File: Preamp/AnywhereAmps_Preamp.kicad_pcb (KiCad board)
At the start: 2 copper layers, 69.1 x 45.2 mm, 59 parts, among them J1 +9V, J2 Battery, J3 VCC, J4 Switch, J5 Pwr LED, J6 POTI, J7 Audio_In, J8 Audio_Out, U1 PTPSM5601R5H, U2 MAX17562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

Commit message: add OSHW logo
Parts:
- added REF**: OSHW-Logo2_9.8x8mm_SilkScreen, Symbol:OSHW-Logo2_9.8x8mm_SilkScreen, F.Cu at (106.9, 141.2)

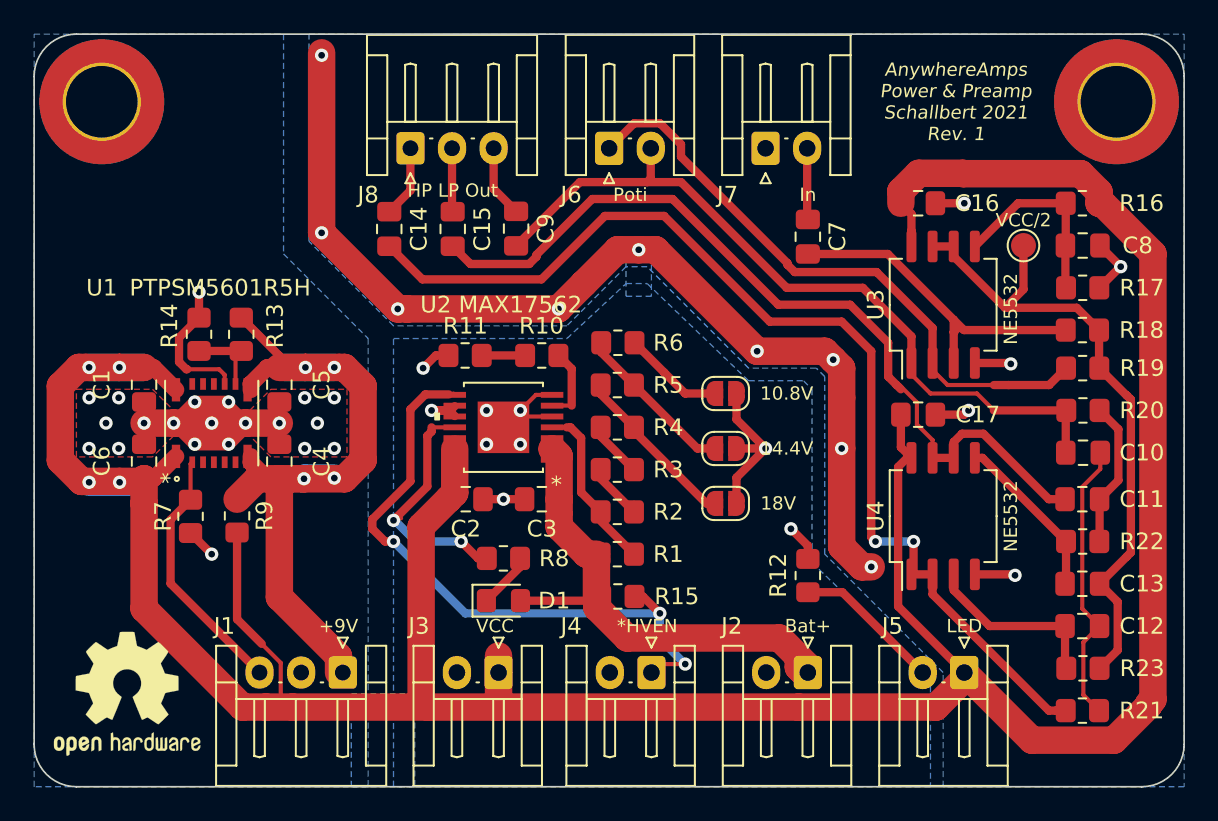
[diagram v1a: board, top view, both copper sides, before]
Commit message: - increate power track size to 2mm - reduce amount of right angles in track design
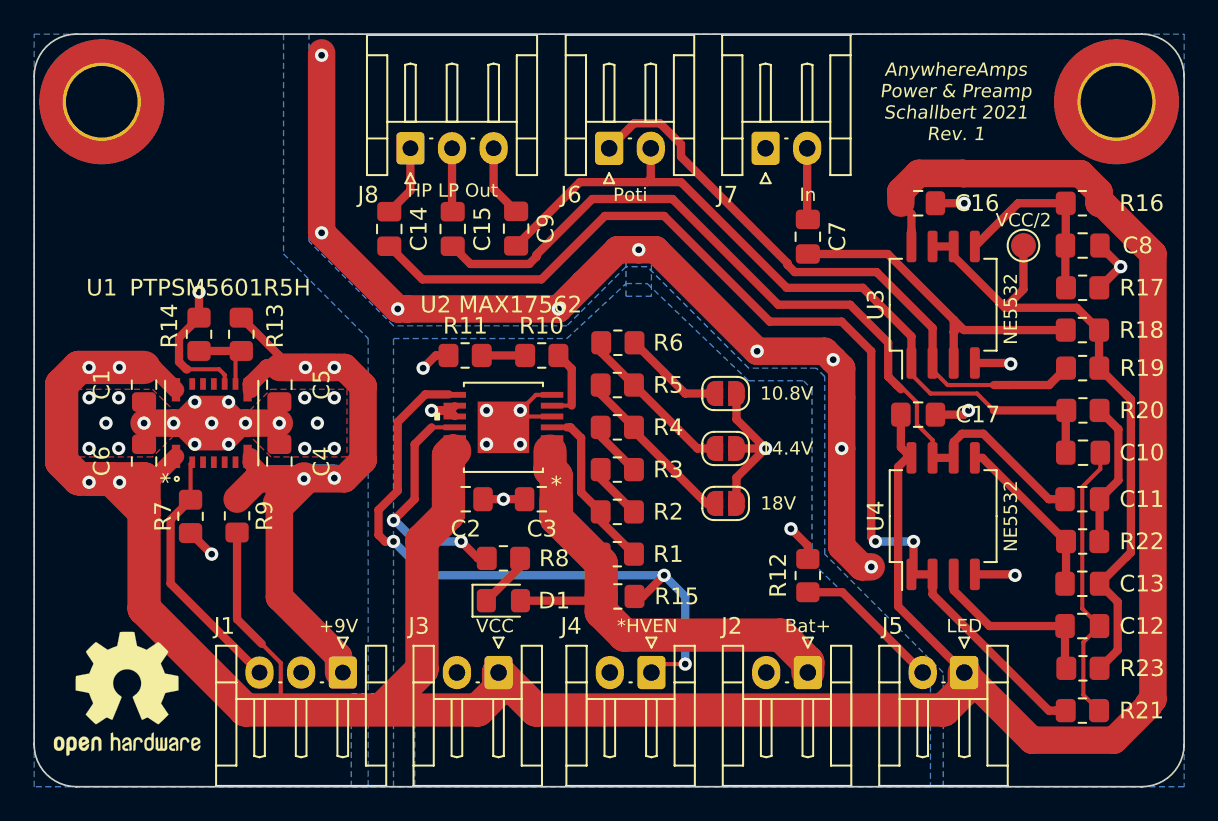
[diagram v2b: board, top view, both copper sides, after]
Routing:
- net VCC: track 202.8 -> 207.2 mm
- net +9V: track 46.8 -> 48.9 mm
- net +BATT: track 33.0 -> 31.1 mm
- net *HVEN: track 38.4 -> 39.8 mm

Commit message: - more 45° edging - update silk screen
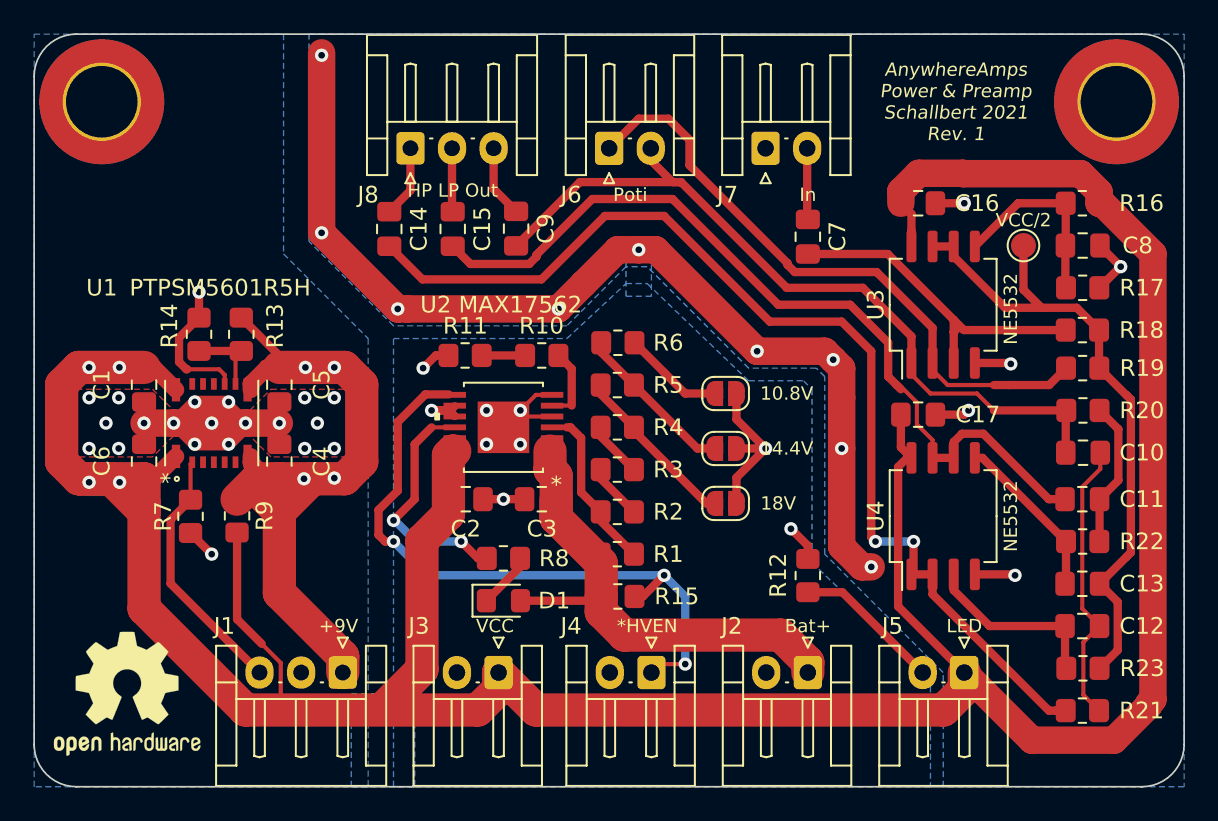
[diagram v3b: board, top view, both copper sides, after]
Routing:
- net +9V: track 48.9 -> 52.5 mm
- net PreampOut: track 46.9 -> 47.9 mm
- net Poti: track 37.0 -> 37.7 mm
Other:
- board text added: "383k -- R1, R7, R9, R15, R16, R17 10k -- R2, R3, R4, R5, R6, R13, R18, R19, R20, R21, R22, R23 1.25k -- R8, R10, R11, R12, R14 22u -- C4, C5 4.7u -- C1, C2, C3, C6, C7, C8, C9, C14, C15 33n -- C10, C11, C12, C13, C16, C17"
- board text removed: "383k -- R1, R7, R9, R15, R16, R17 10k -- R2, R3, R4, R5, R6, R13, R18, R19, R20, R21, R22, R23 1.25k -- R8, R10, R11, R12, R14 4.7u -- C1, C2, C3, C6, C7, C8, C9, C14, C15 22u -- C4, C5 33n -- C10, C11, C12, C13, C16, C17"

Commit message: - switch to polarized capacitors for audio input - increase cap size for bypass on 9V rail - add polarity indicator on silk screen
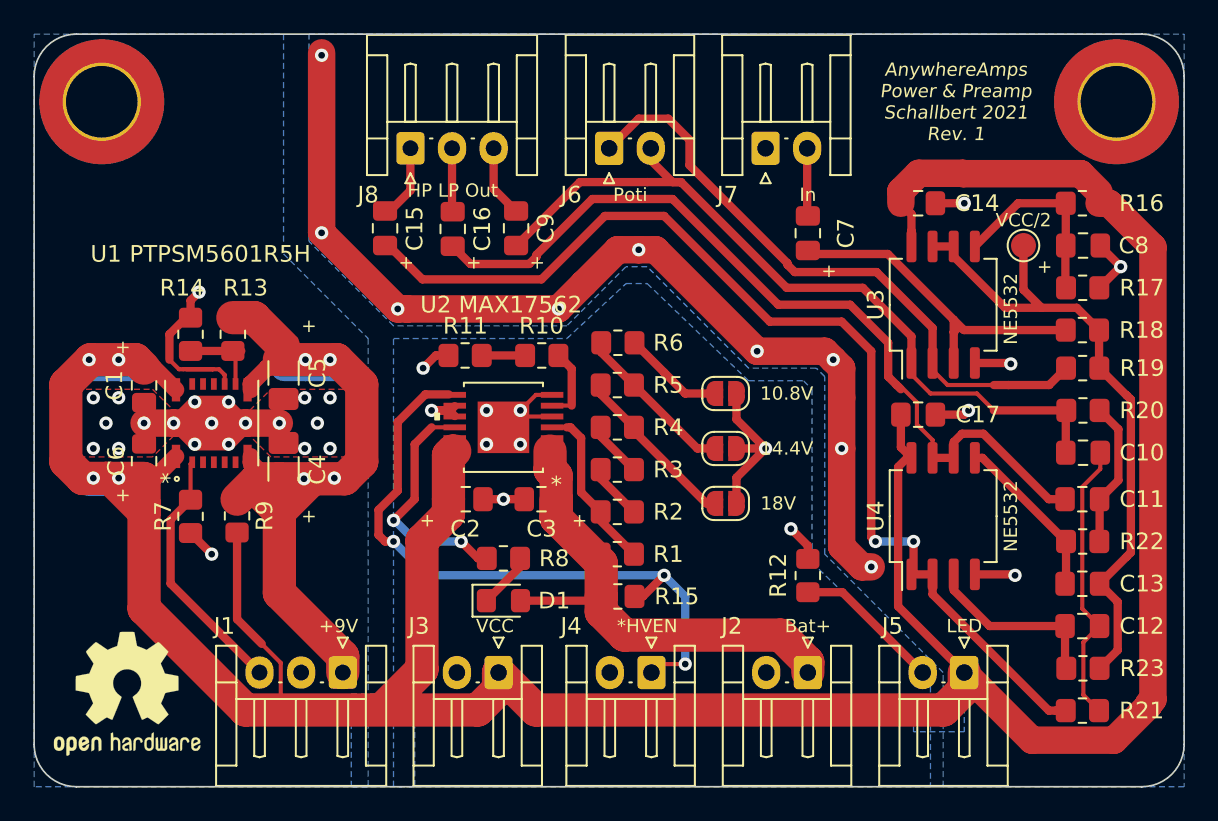
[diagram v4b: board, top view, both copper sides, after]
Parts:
- removed the C14 at (122.7, 113.3)
- added C16: 4.7u, Capacitor_SMD:C_0805_2012Metric_Pad1.18x1.45mm_HandSolder, F.Cu at (126.5, 113.3)
- C4, C5: value 22u -> 47u; footprint Capacitor_SMD:C_0805_2012Metric_Pad1.18x1.45mm_HandSolder -> Capacitor_SMD:C_1206_3216Metric_Pad1.33x1.80mm_HandSolder
- moved C15 4.06 mm to (122.4, 113.3), turned to 90 degrees
- moved C5 0.75 mm to (116.3, 122.0)
- moved C4 0.51 mm to (116.3, 127.7), turned to 90 degrees
- moved R13 0.51 mm to (113.3, 119.6)
- moved R14 0.51 mm to (110.7, 119.6)
- moved C7 0.21 mm to (147.8, 113.6), turned to 90 degrees
- turned C6 to 90 degrees
- renumbered C16 to C14
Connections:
- C15 pad 1: LP_Out -> Net-(C15-Pad1)
- C15 pad 2: Net-(C11-Pad1) -> HP_Out
- C4 pad 1: GND -> +9V
- C4 pad 2: +9V -> GND
- C6 pad 1: GND -> VCC
- C6 pad 2: VCC -> GND
- C7 pad 1: AudioIn -> Net-(C7-Pad1)
- C7 pad 2: Net-(C7-Pad2) -> AudioIn
- R18 pad 1: Net-(C7-Pad2) -> Net-(C7-Pad1)
- R21 pad 2: Net-(C14-Pad2) -> Net-(C15-Pad1)
- U3 pad 3: Net-(C7-Pad2) -> Net-(C7-Pad1)
- U4 pad 1: Net-(C14-Pad2) -> Net-(C15-Pad1)
- U4 pad 2: Net-(C14-Pad2) -> Net-(C15-Pad1)
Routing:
- net Net-(C15-Pad1): track 0.00 -> 67.0 mm, vias 0 -> 2
- net Net-(C14-Pad2): track 67.0 -> 0.00 mm, vias 2 -> 0
- net Net-(C7-Pad2): track 20.6 -> 0.00 mm
- net Net-(C7-Pad1): track 0.00 -> 20.6 mm
- net GND: track 136.2 -> 138.6 mm
- net VCC: track 207.2 -> 205.1 mm
- net +9V: track 52.5 -> 53.2 mm
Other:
- board text added: "+"
- board text added: "383k -- R1, R7, R9, R15, R16, R17 10k -- R2, R3, R4, R5, R6, R13, R18, R19, R20, R21, R22, R23 1.25k -- R8, R10, R11, R12, R14 47u Low ESR Tantalum polarized -- C4, C5 4.7u Low ESR Tantalum polarized -- C1, C2, C3, C6, C7, C8, C9, C14, C15 33n -- C10, C11, C12, C13, C16, C17"
- board text removed: "383k -- R1, R7, R9, R15, R16, R17 10k -- R2, R3, R4, R5, R6, R13, R18, R19, R20, R21, R22, R23 1.25k -- R8, R10, R11, R12, R14 22u -- C4, C5 4.7u -- C1, C2, C3, C6, C7, C8, C9, C14, C15 33n -- C10, C11, C12, C13, C16, C17"

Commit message: - move VCC track away from M4 hole - exchange 383k resistors by E12 390k - use 10k resistors for VGND providers (quicker startup)
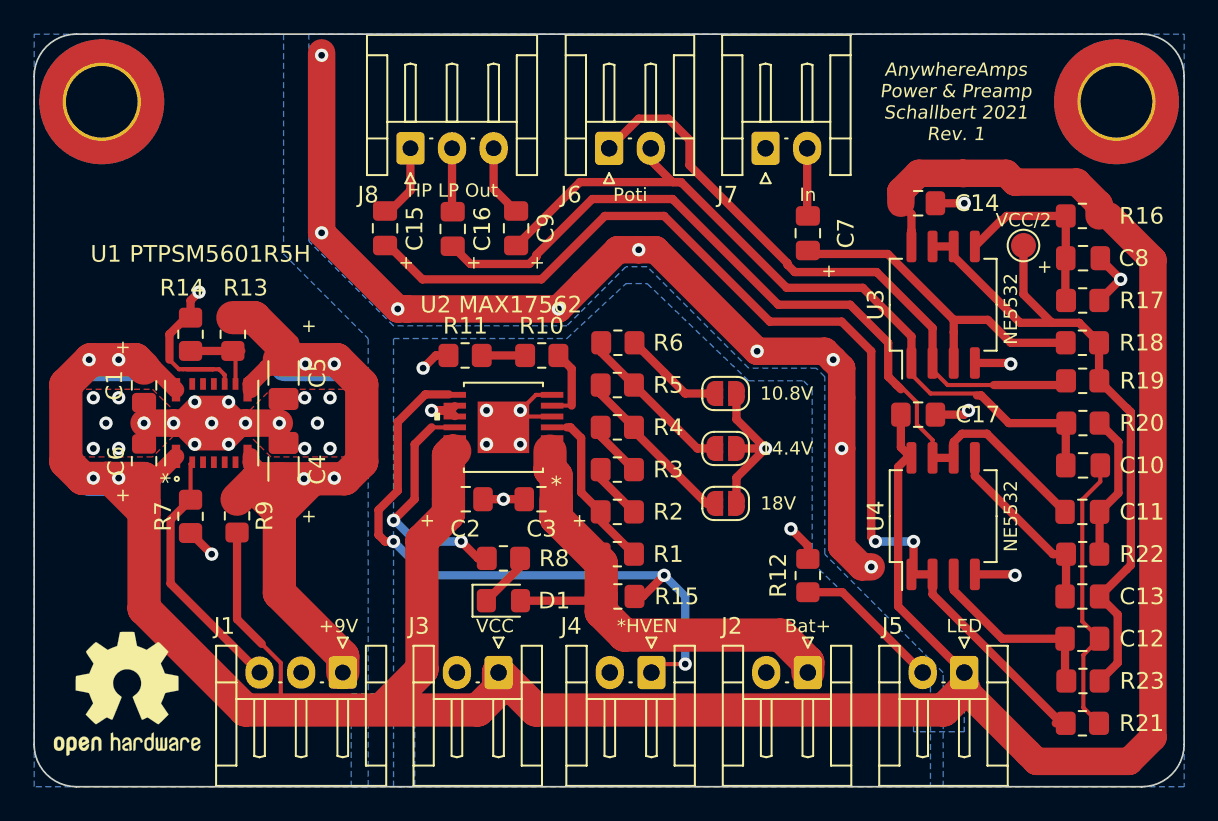
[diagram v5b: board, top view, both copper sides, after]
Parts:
- R1, R15, R7, R9: value 383k -> 390k
- R16, R17: value 383k -> 10k
- moved C10 0.76 mm to (164.4, 127.5)
- moved C11 0.76 mm to (164.3, 130.3)
- moved C12 0.76 mm to (164.3, 137.9)
- moved C13 0.76 mm to (164.3, 135.4)
- moved C8 0.76 mm to (164.4, 115.1)
- moved R16 0.76 mm to (164.3, 112.5)
- moved R17 0.76 mm to (164.3, 117.6)
- moved R18 0.76 mm to (164.3, 120.1)
- moved R19 0.76 mm to (164.3, 122.4)
- moved R20 0.76 mm to (164.4, 125.0)
- moved R21 0.76 mm to (164.3, 143.0)
- moved R22 0.76 mm to (164.3, 132.8)
- moved R23 0.76 mm to (164.4, 140.5)
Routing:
- net VCC: track 205.1 -> 206.7 mm
- net GNDA: track 40.0 -> 41.4 mm
- net Net-(C13-Pad2): track 10.4 -> 11.4 mm
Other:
- board text added: "33n MLCC C10, C11, C12, C13, C14, C17 4.7u low ESR Tantalum C1, C2, C3, C6, C7, C8, C9, C15, C16 47u low ESR Tantalum C4, C5 390k R1, R7, R9, R15 10k R2, R3, R4, R5, R6, R13, R16, R17, R18, R19, R20, R21, R22, R23 1.25k R8, R10, R11, R12, R14"
- board text removed: "383k -- R1, R7, R9, R15, R16, R17 10k -- R2, R3, R4, R5, R6, R13, R18, R19, R20, R21, R22, R23 1.25k -- R8, R10, R11, R12, R14 47u Low ESR Tantalum polarized -- C4, C5 4.7u Low ESR Tantalum polarized -- C1, C2, C3, C6, C7, C8, C9, C14, C15 33n -- C10, C11, C12, C13, C16, C17"
